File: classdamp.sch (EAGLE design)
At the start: 40 parts, among them Q1 BS170, Q2 BS170

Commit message: Just few small things...
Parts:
- removed C3: 47n, resistor:C-EU050-024X044
- added C12: 47n, capacitor-wima:C5/3.5
- C4: value 47n -> 100n; device resistor:C-EU025-025X050 -> capacitor-wima:C2.5/2
- C7: value 1nF -> 1n; device resistor:C-EU025-025X050 -> capacitor-wima:C2.5/2
- C8: device capacitor-wima:C2,5-3 -> capacitor-wima:C2.5/2
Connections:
- net N$11: now also C12.1; no longer C3.1
- net N$13: now also C12.2; no longer C3.2
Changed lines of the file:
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@@
 <part name="D2" library="diode" deviceset="ZENER-DIODE" device="DO34-7" value="6.3V"/>
 <part name="Q2" library="transistor-small-signal" deviceset="BS170" device=""/>
-<part name="C3" library="resistor" deviceset="C-EU" device="050-024X044" value="47n"/>
 <part name="R2" library="resistor" deviceset="R-EU_" device="0204/7" value="1k"/>
-<part name="C4" library="resistor" deviceset="C-EU" device="025-025X050" value="47n"/>
 <part name="JP3" library="pinhead" deviceset="PINHD-1X2" device=""/>
 <part name="JP4" library="pinhead" deviceset="PINHD-1X2" device="" value="Audio_In"/>
@@
 <part name="C6" library="resistor" deviceset="CPOL-EU" device="E1.8-4" value="10uF"/>
 <part name="R5" library="resistor" deviceset="R-EU_" device="0204/2V" value="10k"/>
-<part name="C7" library="resistor" deviceset="C-EU" device="025-025X050" value="1nF"/>
 <part name="U$1" library="avr-7" deviceset="TINY26" device="P"/>
-<part name="C8" library="capacitor-wima" deviceset="C" device="2,5-3" value="100n"/>
+<part name="C8" library="capacitor-wima" deviceset="C" device="2.5/2" value="100n"/>
 <part name="C9" library="capacitor-wima" deviceset="C" device="2.5/2" value="100n"/>
 <part name="C10" library="capacitor-wima" deviceset="C" device="2.5/2" value="100n"/>
@@
 <part name="JP1" library="pinhead" deviceset="PINHD-1X2" device="" value="On/Off"/>
 <part name="GND7" library="supply1" deviceset="GND" device=""/>
+<part name="C4" library="capacitor-wima" deviceset="C" device="2.5/2" value="100n"/>
+<part name="C7" library="capacitor-wima" deviceset="C" device="2.5/2" value="1n"/>
+<part name="C12" library="capacitor-wima" deviceset="C" device="5/3.5" value="47n"/>
 </parts>
 <sheets>
@@
 <instance part="D2" gate="G$1" x="167.64" y="60.96" rot="R90"/>
 <instance part="Q2" gate="1" x="165.1" y="45.72"/>
-<instance part="C3" gate="G$1" x="182.88" y="93.98" rot="R90"/>
 <instance part="R2" gate="G$1" x="167.64" y="73.66" rot="R90"/>
-<instance part="C4" gate="G$1" x="25.4" y="-53.34" rot="R90"/>
 <instance part="JP3" gate="G$1" x="-30.48" y="81.28" rot="MR0"/>
 <instance part="JP4" gate="G$1" x="7.62" y="-7.62" rot="MR0"/>
@@
 <instance part="C6" gate="G$1" x="17.78" y="2.54"/>
 <instance part="R5" gate="G$1" x="48.26" y="0"/>
-<instance part="C7" gate="G$1" x="53.34" y="-5.08"/>
 <instance part="U$1" gate="G$1" x="-5.08" y="-40.64"/>
 <instance part="C8" gate="G$1" x="-43.18" y="-48.26"/>
@@
 <instance part="JP1" gate="G$1" x="190.5" y="-15.24" rot="MR0"/>
 <instance part="GND7" gate="1" x="203.2" y="-20.32"/>
+<instance part="C4" gate="G$1" x="25.4" y="-53.34" rot="R90"/>
+<instance part="C7" gate="G$1" x="53.34" y="-5.08"/>
+<instance part="C12" gate="G$1" x="182.88" y="93.98" rot="R90"/>
 </instances>
 <busses>
@@
 <wire x1="152.4" y1="-2.54" x2="152.4" y2="-15.24" width="0.1524" layer="91"/>
 <junction x="152.4" y="-15.24"/>
-<pinref part="C7" gate="G$1" pin="2"/>
 <wire x1="53.34" y1="-10.16" x2="53.34" y2="-15.24" width="0.1524" layer="91"/>
 <pinref part="JP7" gate="A" pin="3"/>
@@
 <wire x1="157.48" y1="-15.24" x2="157.48" y2="-10.16" width="0.1524" layer="91"/>
 <pinref part="GND4" gate="1" pin="GND"/>
+<pinref part="C7" gate="G$1" pin="2"/>
 </segment>
 <segment>
@@
 </segment>
 <segment>
-<pinref part="C4" gate="G$1" pin="2"/>
 <pinref part="GND1" gate="1" pin="GND"/>
 <wire x1="30.48" y1="-53.34" x2="45.72" y2="-53.34" width="0.1524" layer="91"/>
+<pinref part="C4" gate="G$1" pin="2"/>
 </segment>
 <segment>
@@
 <pinref part="Q9" gate="G$1" pin="D"/>
 <pinref part="Q7" gate="G$1" pin="D"/>
-<pinref part="C3" gate="G$1" pin="1"/>
 <wire x1="180.34" y1="93.98" x2="177.8" y2="93.98" width="0.1524" layer="91"/>
 <wire x1="177.8" y1="93.98" x2="177.8" y2="104.14" width="0.1524" layer="91"/>
@@
 <pinref part="X1" gate="-2" pin="KL"/>
 <wire x1="157.48" y1="93.98" x2="177.8" y2="93.98" width="0.1524" layer="91"/>
+<pinref part="C12" gate="G$1" pin="1"/>
 </segment>
 </net>
@@
 <wire x1="187.96" y1="60.96" x2="203.2" y2="60.96" width="0.1524" layer="91"/>
 <wire x1="203.2" y1="60.96" x2="203.2" y2="93.98" width="0.1524" layer="91"/>
-<pinref part="C3" gate="G$1" pin="2"/>
 <wire x1="203.2" y1="93.98" x2="190.5" y2="93.98" width="0.1524" layer="91"/>
 <wire x1="190.5" y1="93.98" x2="187.96" y2="93.98" width="0.1524" layer="91"/>
@@
 <pinref part="Q8" gate="G$1" pin="D"/>
 <pinref part="X1" gate="-1" pin="KL"/>
+<pinref part="C12" gate="G$1" pin="2"/>
 </segment>
 </net>
@@
 <pinref part="R5" gate="G$1" pin="2"/>
 <wire x1="53.34" y1="0" x2="63.5" y2="0" width="0.1524" layer="91"/>
-<pinref part="C7" gate="G$1" pin="1"/>
 <wire x1="53.34" y1="-2.54" x2="53.34" y2="0" width="0.1524" layer="91"/>
 <label x="63.5" y="0" size="1.778" layer="95" rot="MR0"/>
+<pinref part="C7" gate="G$1" pin="1"/>
 </segment>
 <segment>
@@
 <segment>
 <pinref part="U$1" gate="G$1" pin="(AREF)PA3"/>
+<wire x1="17.78" y1="-53.34" x2="22.86" y2="-53.34" width="0.1524" layer="91"/>
 <pinref part="C4" gate="G$1" pin="1"/>
-<wire x1="17.78" y1="-53.34" x2="22.86" y2="-53.34" width="0.1524" layer="91"/>
-</segment>
-</net>
+</segment>
+</net>

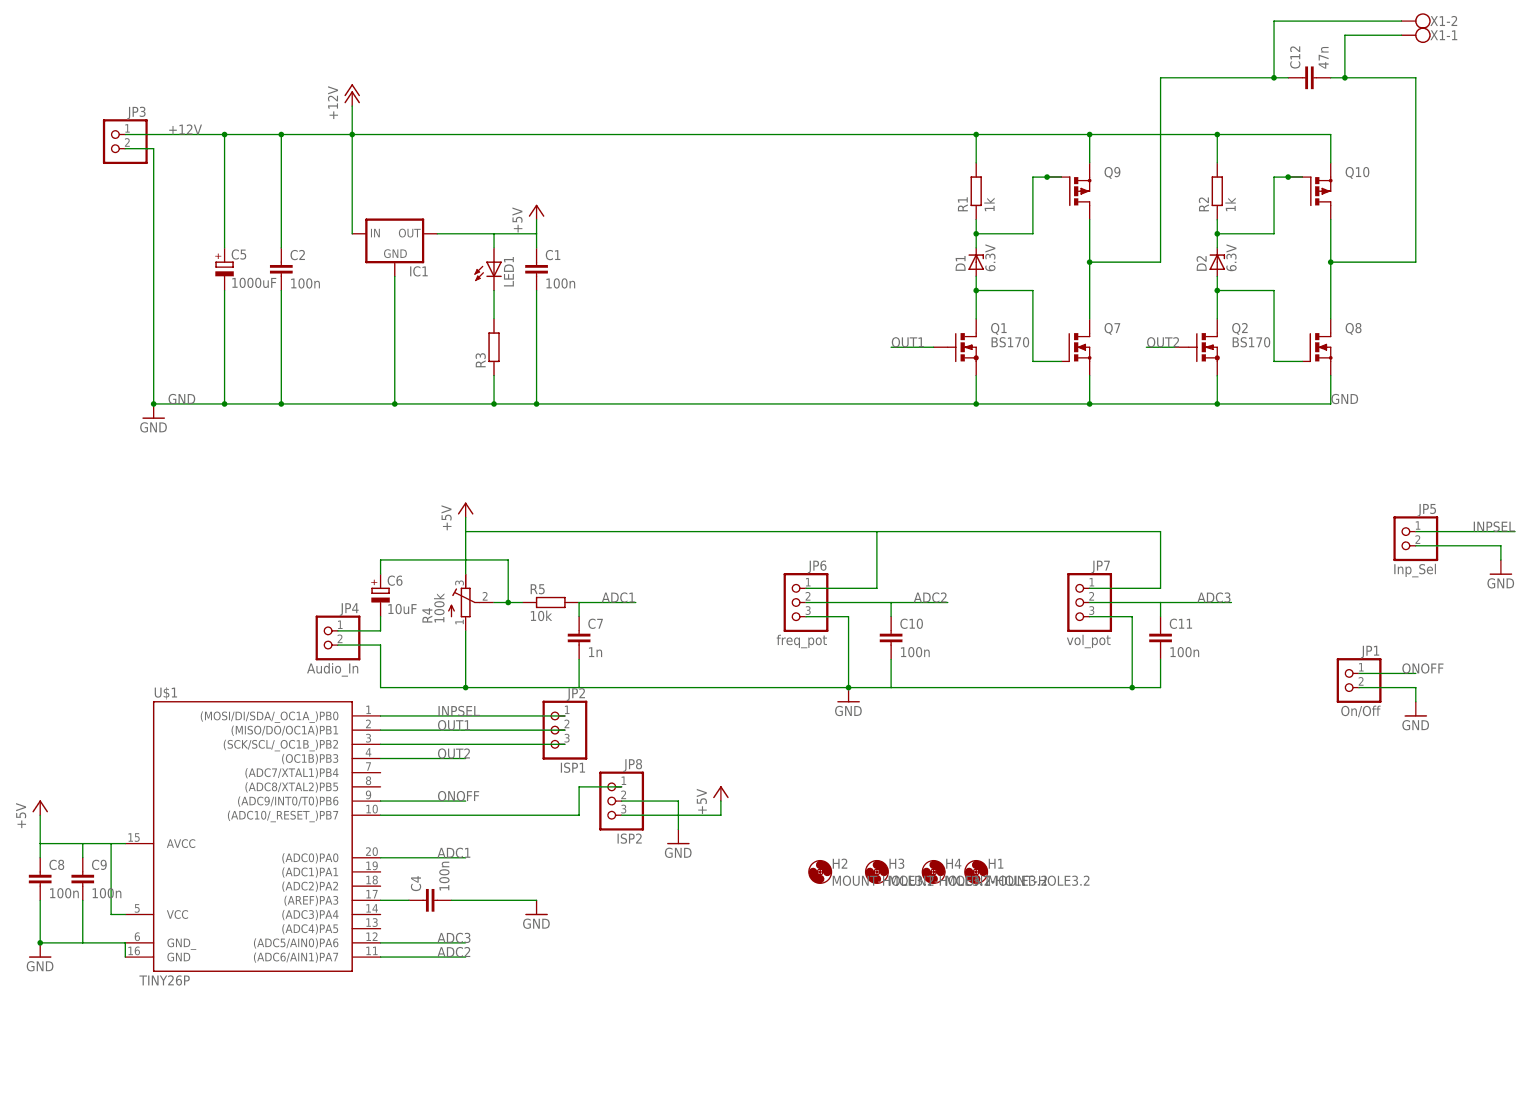
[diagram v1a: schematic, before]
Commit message: R/C durch SMD ersetzt - bessere GND-Flächen
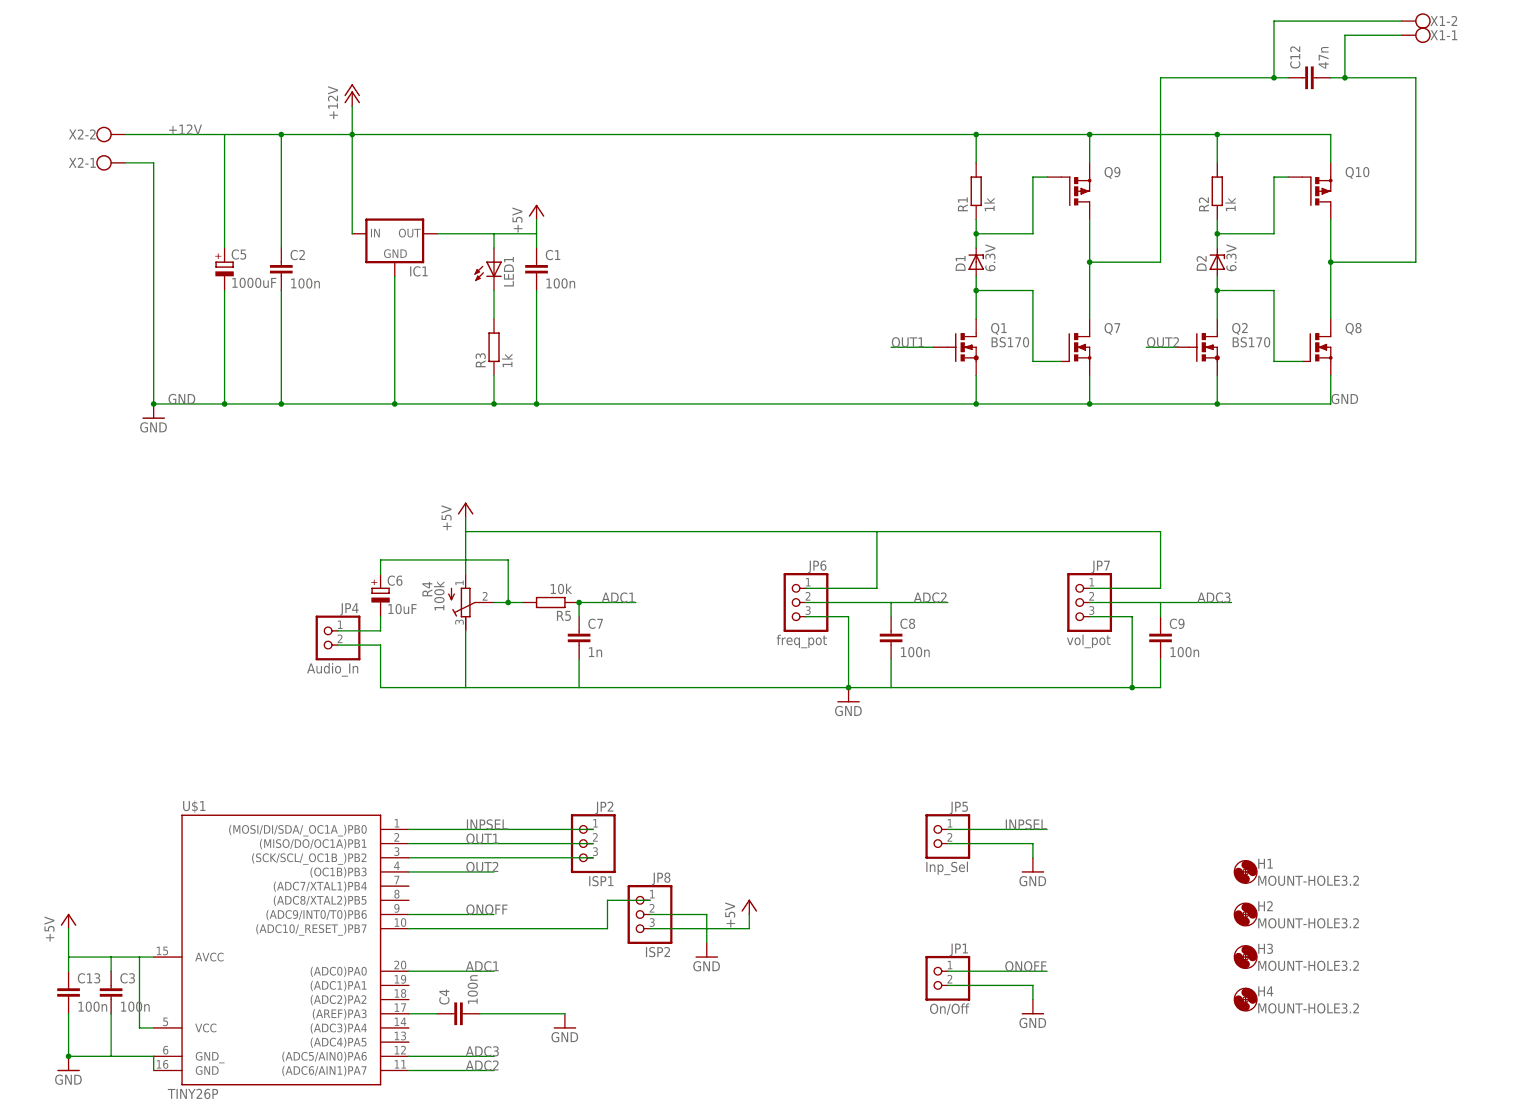
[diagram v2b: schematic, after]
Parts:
- removed C10, C11: 100n, capacitor-wima:C2.5/2
- removed JP3: (no value), pinhead:PINHD-1X2
- added C13, C3: 100n, resistor:C-EUC0805K
- added X2: (no value), con-wago-500:W237-102
- C1, C4, C7, C8, C9: device capacitor-wima:C2.5/2 -> resistor:C-EUC0805K
- C2: device capacitor-wima:C2,5-3 -> resistor:C-EUC0805K
- D1, D2: device diode:ZENER-DIODEDO34-7 -> diode:ZENER-DIODEZD-12.5
- R1, R2: device resistor:R-EU_0204/7 -> resistor:R-EU_R0805
- R3: value (none) -> 1k; device resistor:R-EU_0204/7 -> resistor:R-EU_R0805
- R5: device resistor:R-EU_0204/2V -> resistor:R-EU_R0805
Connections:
- net +12V: now also X2-2.KL; no longer JP3.1
- net +5V: now also C13.1, C3.1, R4.E; no longer C8.1, C9.1, R4.A
- net ADC1: now also R5.1; no longer R5.2
- net ADC2: now also C8.1; no longer C10.1
- net ADC3: now also C9.1; no longer C11.1
- net GND: now also C13.2, C3.2, R4.A, X2-1.KL; no longer C10.2, C11.2, JP3.2, R4.E
- net N$10: now also R5.2; no longer R5.1
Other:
- moved on the sheet: C4, C8, C9, H1, H2, H3, H4, JP1, JP2, JP5, JP8, R4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

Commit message: few details
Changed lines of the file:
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@@
 <wire x1="27.94" y1="66.04" x2="38.1" y2="66.04" width="0.1524" layer="91"/>
 <pinref part="C1" gate="G$1" pin="1"/>
+<junction x="38.1" y="66.04"/>
+<junction x="45.72" y="66.04"/>
 </segment>
 <segment>
@@
 <pinref part="R4" gate="G$1" pin="E"/>
 <wire x1="33.02" y1="5.08" x2="33.02" y2="12.7" width="0.1524" layer="91"/>
+<junction x="33.02" y="12.7"/>
+<junction x="106.68" y="12.7"/>
 </segment>
 <segment>
@@
 <pinref part="C3" gate="G$1" pin="1"/>
 <pinref part="C13" gate="G$1" pin="1"/>
+<junction x="-25.4" y="-63.5"/>
+<junction x="-30.48" y="-63.5"/>
+<junction x="-38.1" y="-63.5"/>
 </segment>
 <segment>
@@
 <wire x1="-10.16" y1="83.82" x2="-27.94" y2="83.82" width="0.1524" layer="91"/>
 <pinref part="C2" gate="G$1" pin="1"/>
+<junction x="-10.16" y="83.82"/>
 </segment>
 </net>
@@
 <wire x1="33.02" y1="-5.08" x2="33.02" y2="-15.24" width="0.1524" layer="91"/>
 <pinref part="C7" gate="G$1" pin="2"/>
+<junction x="33.02" y="-15.24"/>
+<junction x="53.34" y="-15.24"/>
+<junction x="109.22" y="-15.24"/>
 </segment>
 <segment>
@@
 <pinref part="C3" gate="G$1" pin="2"/>
 <pinref part="C13" gate="G$1" pin="2"/>
+<junction x="-30.48" y="-81.28"/>
+<junction x="-22.86" y="-81.28"/>
 </segment>
 <segment>
@@
 <wire x1="157.48" y1="0" x2="157.48" y2="-2.54" width="0.1524" layer="91"/>
 <pinref part="C9" gate="G$1" pin="1"/>
+<junction x="157.48" y="0"/>
 </segment>
 <segment>
@@
 <wire x1="109.22" y1="0" x2="109.22" y2="-2.54" width="0.1524" layer="91"/>
 <pinref part="C8" gate="G$1" pin="1"/>
-</segment>
-<segment>
+<junction x="109.22" y="0"/>
+</segment>
+<segment>

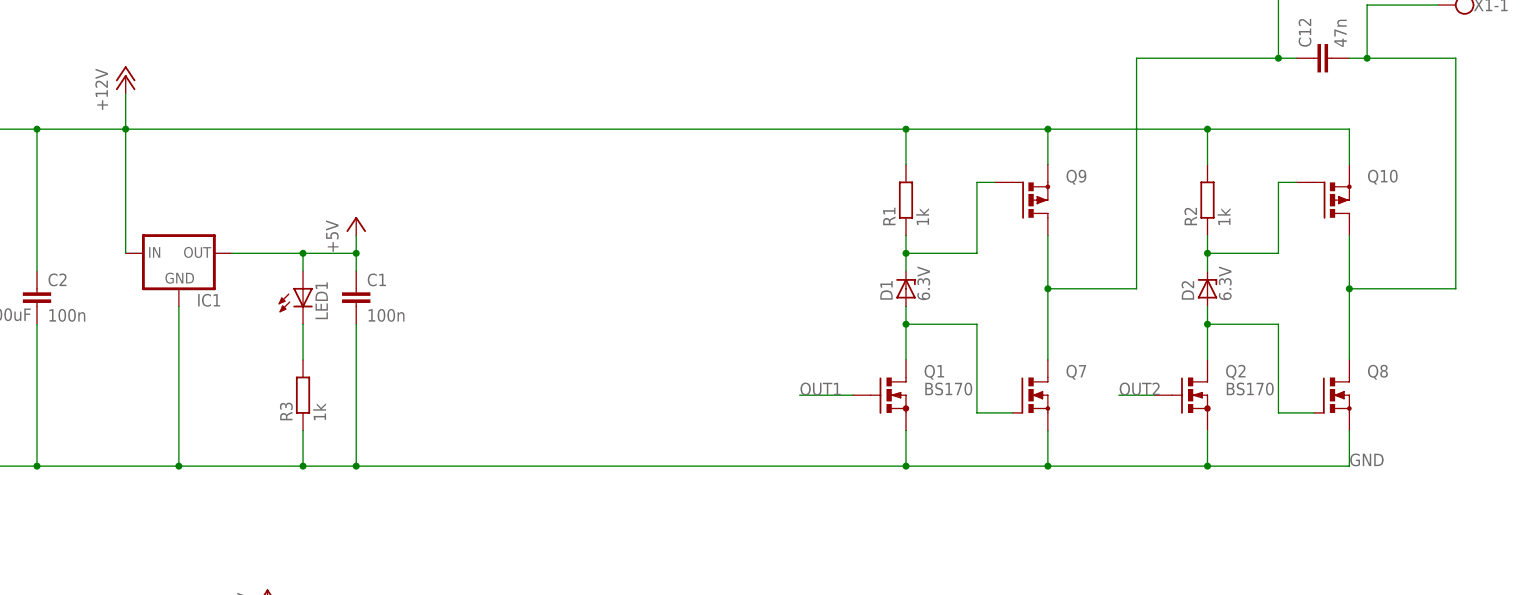
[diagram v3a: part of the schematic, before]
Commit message: added partlist
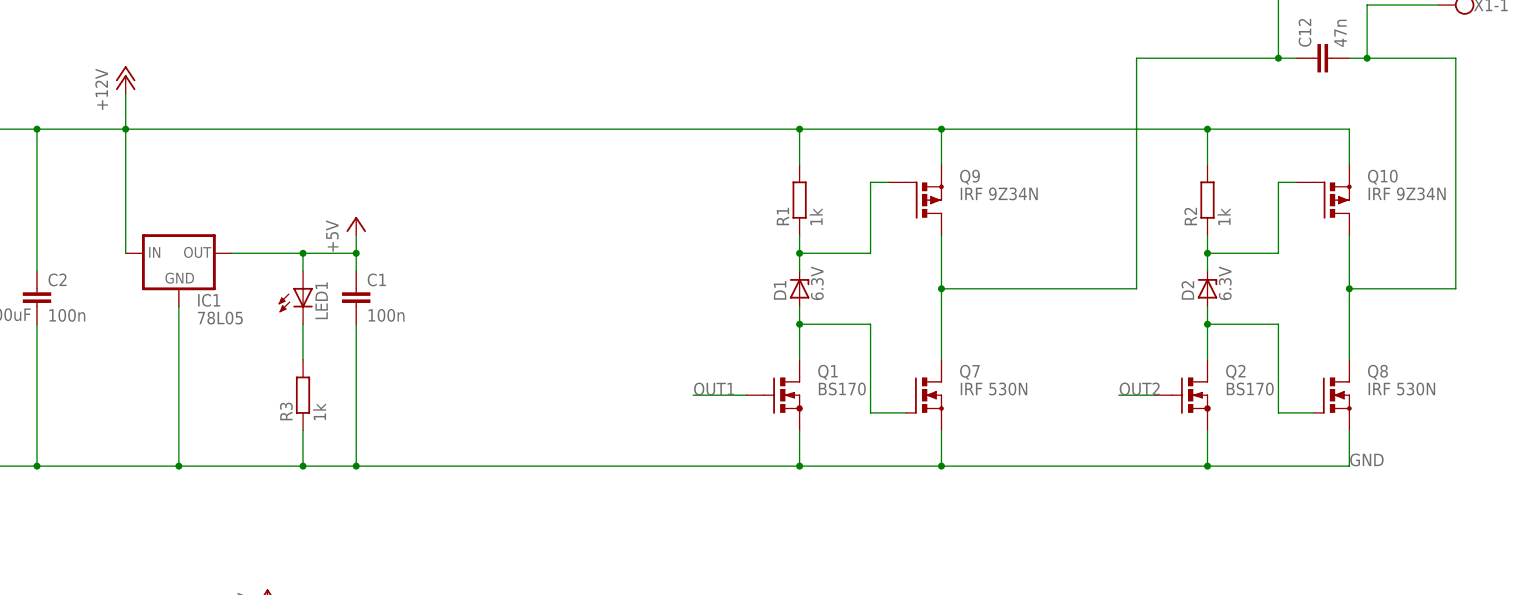
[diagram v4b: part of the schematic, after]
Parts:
- IC1: value (none) -> 78L05
- Q10, Q9: value (none) -> IRF 9Z34N
- Q7, Q8: value (none) -> IRF 530N
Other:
- moved on the sheet: D1, Q1, Q7, Q9, R1
